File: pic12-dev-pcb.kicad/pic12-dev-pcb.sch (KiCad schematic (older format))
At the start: 8 parts, among them J1 PGM-Conn, J2 App-Conn1, J3 App-Conn2, U1 PIC12F675-ISN

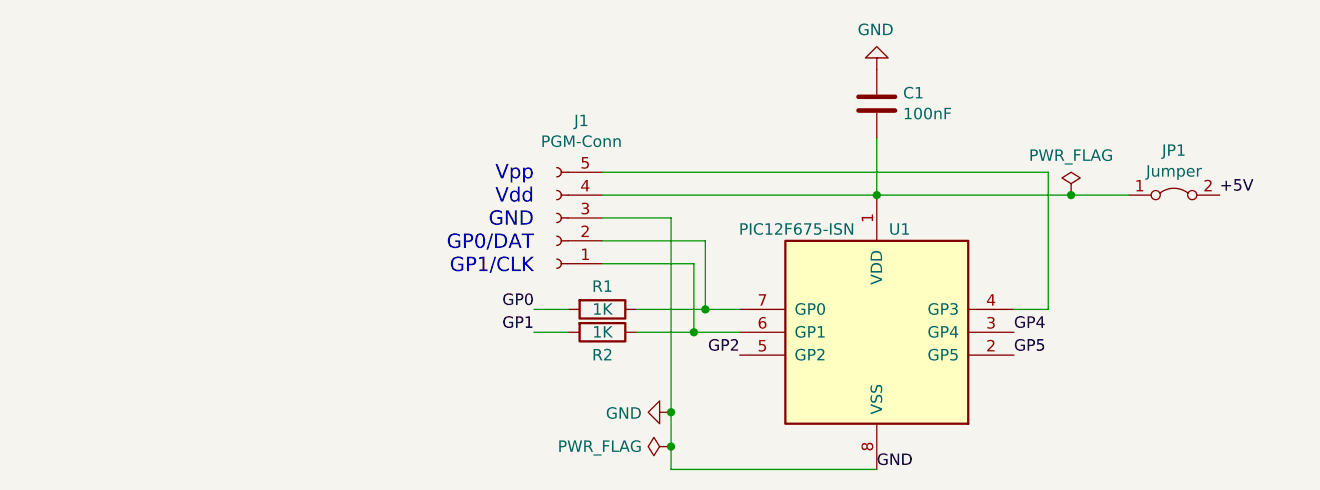
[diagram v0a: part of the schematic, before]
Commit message: added SR-connector
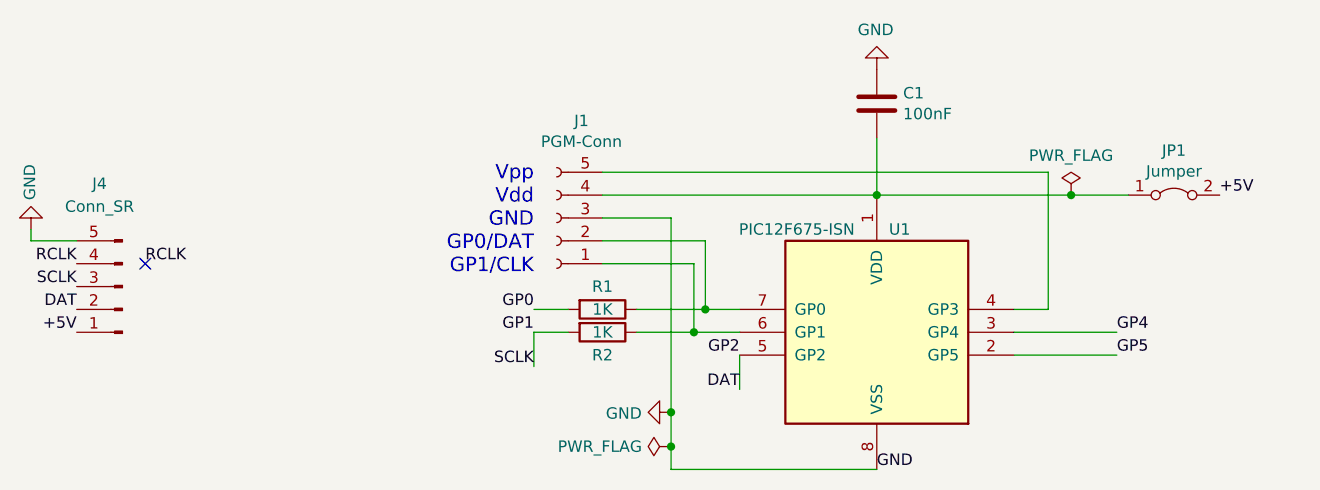
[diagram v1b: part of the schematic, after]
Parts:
- added J4: Conn_SR, Connector_PinHeader_2.54mm:PinHeader_1x05_P2.54mm_Vertical, symbol Connector:Conn_01x05_Male
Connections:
- net +5V: now also J4.1 (Pin_1)
- net GND: now also J4.5 (Pin_5)
- net GP1: now also J4.3 (Pin_3)
- net GP2 renamed DAT
- net DAT: now also J4.2 (Pin_2)
- new net RCLK: J4.4 (Pin_4)
- no-connect marks 0 -> 1
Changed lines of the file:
@@
 Sheet 1 1
 Title "PIC12-Development Breadboard-PCB"
-Date "2020-08-30"
+Date "2020-08-31"
 Rev "1"
 Comp "Bernhard Bablok"
@@
 Text Label 7850 3900 2    50   ~ 0
 GP2
-Text Label 6350 3550 0    50   ~ 0
+Text Label 6800 3550 0    50   ~ 0
 GP4
-Text Label 6350 3650 0    50   ~ 0
+Text Label 6800 3650 0    50   ~ 0
 GP5
 Text Label 5150 3650 2    50   ~ 0
@@
 Text Label 9000 3900 0    50   ~ 0
 GP2
+$Comp
+L Connector:Conn_01x05_Male J4
+U 1 1 5F4D3DB1
+P 2450 3350
+F 0 "J4" H 2550 2900 50  0000 C CNN
+F 1 "Conn_SR" H 2550 3000 50  0000 C CNN
+F 2 "Connector_PinHeader_2.54mm:PinHeader_1x05_P2.54mm_Vertical" H 2450 3350 50  0001 C CNN
+F 3 "~" H 2450 3350 50  0001 C CNN
+	1    2450 3350
+	-1   0    0    1
+$EndComp
+$Comp
+L power:GND #PWR0103
+U 1 1 5F4D4AE2
+P 2050 3100
+F 0 "#PWR0103" H 2050 2850 50  0001 C CNN
+F 1 "GND" V 2055 2972 50  0000 R CNN
+F 2 "" H 2050 3100 50  0001 C CNN
+F 3 "" H 2050 3100 50  0001 C CNN
+	1    2050 3100
+	-1   0    0    1
+$EndComp
+Text Label 2250 3250 2    50   ~ 0
+RCLK
+Text Label 2250 3350 2    50   ~ 0
+SCLK
+Text Label 2250 3450 2    50   ~ 0
+DAT
+Text Label 2250 3550 2    50   ~ 0
++5V
+Wire Wire Line
+	2250 3150 2050 3150
+Wire Wire Line
+	2050 3150 2050 3100
+Wire Wire Line
+	6350 3650 6800 3650
+Wire Wire Line
+	6350 3550 6800 3550
+Text Label 5150 3800 2    50   ~ 0
+DAT
+Wire Wire Line
+	5150 3800 5150 3650
+Text Label 4250 3700 2    50   ~ 0
+SCLK
+Wire Wire Line
+	4250 3700 4250 3550
+Text Label 2550 3250 0    50   ~ 0
+RCLK
+NoConn ~ 2550 3250
 $EndSCHEMATC

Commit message: fix labeling of GP2 net, add USB-connector
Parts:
- added J5: USB_B_Micro, symbol Connector:USB_B_Micro
- added J6: Conn_BB1, Connector_PinHeader_2.54mm:PinHeader_2x01_P2.54mm_Horizontal, symbol Connector:Conn_01x02_Male
- added J7: Conn_BB2, Connector_PinHeader_2.54mm:PinHeader_2x01_P2.54mm_Horizontal, symbol Connector:Conn_01x02_Male
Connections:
- net labels removed: DAT
- wire segments 28 -> 37
- no-connect marks 1 -> 4
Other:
- note added: "SERin"
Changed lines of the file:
@@
 Title "PIC12-Development Breadboard-PCB"
 Date "2020-09-07"
-Rev "2"
+Rev "3"
 Comp "Bernhard Bablok"
 Comment1 "https://github.com/bablokb/pcb-pic-devboard"
@@
 $EndComp
 $Comp
-L power:PWR_FLAG #FLG0102
-U 1 1 5F05C8DC
-P 4850 4050
-F 0 "#FLG0102" H 4850 4125 50  0001 C CNN
-F 1 "PWR_FLAG" V 4850 4177 50  0000 L CNN
-F 2 "" H 4850 4050 50  0001 C CNN
-F 3 "~" H 4850 4050 50  0001 C CNN
-	1    4850 4050
-	0    -1   -1   0
-$EndComp
-Connection ~ 4850 4050
-Wire Wire Line
-	4850 4050 4850 4150
-$Comp
 L Device:C C1
 U 1 1 5F062C50
@@
 L power:GND #PWR0102
 U 1 1 5F0642E9
-P 4850 3900
-F 0 "#PWR0102" H 4850 3650 50  0001 C CNN
-F 1 "GND" V 4855 3772 50  0000 R CNN
-F 2 "" H 4850 3900 50  0001 C CNN
-F 3 "" H 4850 3900 50  0001 C CNN
-	1    4850 3900
+P 5150 5300
+F 0 "#PWR0102" H 5150 5050 50  0001 C CNN
+F 1 "GND" V 5155 5172 50  0000 R CNN
+F 2 "" H 5150 5300 50  0001 C CNN
+F 3 "" H 5150 5300 50  0001 C CNN
+	1    5150 5300
 	0    1    1    0
 $EndComp
@@
 	0    1    1    0
 $EndComp
-Connection ~ 4850 3900
-Wire Wire Line
-	4850 3900 4850 4050
 Wire Wire Line
 	4250 3450 4400 3450
-Wire Wire Line
-	4850 3050 4850 3900
 Wire Wire Line
 	4250 3550 4400 3550
@@
 SCLK
 Text Label 2250 3450 2    50   ~ 0
-DAT
+GP2
 Text Label 2250 3550 2    50   ~ 0
 +5V
@@
 Wire Wire Line
 	6350 3550 6800 3550
-Text Label 5150 3800 2    50   ~ 0
-DAT
-Wire Wire Line
-	5150 3800 5150 3650
 Text Label 4250 3700 2    50   ~ 0
 SCLK
@@
 RCLK
 NoConn ~ 2550 3250
+Text Notes 1850 3450 0    50   ~ 0
+SERin
+$Comp
+L Connector:USB_B_Micro J5
+U 1 1 5F569D9B
+P 5900 5300
+F 0 "J5" V 5911 5630 50  0000 L CNN
+F 1 "USB_B_Micro" V 6002 5630 50  0000 L CNN
+F 2 "" H 6050 5250 50  0001 C CNN
+F 3 "~" H 6050 5250 50  0001 C CNN
+	1    5900 5300
+	0    1    1    0
+$EndComp
+NoConn ~ 5700 5600
+NoConn ~ 5800 5600
+NoConn ~ 5900 5600
+Text Label 6200 5700 0    50   ~ 0
++5V
+Wire Wire Line
+	6200 5700 6100 5700
+Wire Wire Line
+	6100 5700 6100 5600
+Wire Wire Line
+	5500 5300 5400 5300
+Wire Wire Line
+	5500 5200 5400 5200
+Wire Wire Line
+	5400 5200 5400 5300
+Connection ~ 5400 5300
+Wire Wire Line
+	4850 3050 4850 4150
+Wire Wire Line
+	5150 5300 5400 5300
+$Comp
+L Connector:Conn_01x02_Male J6
+U 1 1 5F57072D
+P 1950 4500
+F 0 "J6" H 2050 4800 50  0000 C CNN
+F 1 "Conn_BB1" H 2050 4650 50  0000 C CNN
+F 2 "Connector_PinHeader_2.54mm:PinHeader_2x01_P2.54mm_Horizontal" H 1950 4500 50  0001 C CNN
+F 3 "~" H 1950 4500 50  0001 C CNN
+	1    1950 4500
+	1    0    0    -1
+$EndComp
+$Comp
+L Connector:Conn_01x02_Male J7
+U 1 1 5F570C00
+P 2750 4600
+F 0 "J7" H 2900 4250 50  0000 R CNN
+F 1 "Conn_BB2" H 2950 4350 50  0000 R CNN
+F 2 "Connector_PinHeader_2.54mm:PinHeader_2x01_P2.54mm_Horizontal" H 2750 4600 50  0001 C CNN
+F 3 "~" H 2750 4600 50  0001 C CNN
+	1    2750 4600
+	-1   0    0    1
+$EndComp
+$Comp
+L power:GND #PWR0104
+U 1 1 5F5716E2
+P 2400 4750
+F 0 "#PWR0104" H 2400 4500 50  0001 C CNN
+F 1 "GND" V 2405 4622 50  0000 R CNN
+F 2 "" H 2400 4750 50  0001 C CNN
+F 3 "" H 2400 4750 50  0001 C CNN
+	1    2400 4750
+	0    -1   -1   0
+$EndComp
+Text Label 2250 4750 2    50   ~ 0
++5V
+Wire Wire Line
+	2250 4750 2250 4600
+Wire Wire Line
+	2250 4600 2150 4600
+Wire Wire Line
+	2250 4600 2550 4600
+Connection ~ 2250 4600
+Wire Wire Line
+	2400 4750 2400 4500
+Wire Wire Line
+	2400 4500 2550 4500
+Wire Wire Line
+	2400 4500 2150 4500
+Connection ~ 2400 4500
 $EndSCHEMATC

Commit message: swap GP0-GP2, add micro-USB breakout
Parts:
- removed J5: USB_B_Micro, symbol Connector:USB_B_Micro
- removed J7: Conn_BB2, Connector_PinHeader_2.54mm:PinHeader_2x01_P2.54mm_Horizontal, symbol Connector:Conn_01x02_Male
- added USB1: Micro-USB_Breakout, user:Micro-USB_Breakout, symbol User:Micro-USB_Breakout
- J1: footprint Connector_PinHeader_2.54mm:PinHeader_1x05_P2.54mm_Vertical -> Connector_PinSocket_2.54mm:PinSocket_1x05_P2.54mm_Vertical
- J6: footprint Connector_PinHeader_2.54mm:PinHeader_2x01_P2.54mm_Horizontal -> Connector_PinHeader_2.54mm:PinHeader_1x02_P2.54mm_Horizontal
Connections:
- wire segments 37 -> 33
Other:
- moved on the sheet: J6
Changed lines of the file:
@@
 Sheet 1 1
 Title "PIC12-Development Breadboard-PCB"
-Date "2020-09-07"
+Date "2020-09-19"
 Rev "3"
 Comp "Bernhard Bablok"
@@
 F 0 "J1" H 4242 2625 50  0000 C CNN
 F 1 "PGM-Conn" H 4242 2716 50  0000 C CNN
-F 2 "Connector_PinHeader_2.54mm:PinHeader_1x05_P2.54mm_Vertical" H 4350 3050 50  0001 C CNN
+F 2 "Connector_PinSocket_2.54mm:PinSocket_1x05_P2.54mm_Vertical" H 4350 3050 50  0001 C CNN
 F 3 "~" H 4350 3050 50  0001 C CNN
 	1    4350 3050
@@
 L power:GND #PWR0102
 U 1 1 5F0642E9
-P 5150 5300
-F 0 "#PWR0102" H 5150 5050 50  0001 C CNN
-F 1 "GND" V 5155 5172 50  0000 R CNN
-F 2 "" H 5150 5300 50  0001 C CNN
-F 3 "" H 5150 5300 50  0001 C CNN
-	1    5150 5300
+P 5600 4750
+F 0 "#PWR0102" H 5600 4500 50  0001 C CNN
+F 1 "GND" V 5605 4622 50  0000 R CNN
+F 2 "" H 5600 4750 50  0001 C CNN
+F 3 "" H 5600 4750 50  0001 C CNN
+	1    5600 4750
 	0    1    1    0
 $EndComp
@@
 Text Label 7850 3600 2    50   ~ 0
 GND
-Text Label 7850 3700 2    50   ~ 0
+Text Label 7850 3900 2    50   ~ 0
 GP0
 Text Label 7850 3800 2    50   ~ 0
 GP1
-Text Label 7850 3900 2    50   ~ 0
+Text Label 7850 3700 2    50   ~ 0
 GP2
 Text Label 6800 3550 0    50   ~ 0
@@
 Text Label 8500 3600 2    50   ~ 0
 GND
-Text Label 8500 3700 2    50   ~ 0
+Text Label 8500 3900 2    50   ~ 0
 GP0
 Text Label 8500 3800 2    50   ~ 0
 GP1
-Text Label 8500 3900 2    50   ~ 0
+Text Label 8500 3700 2    50   ~ 0
 GP2
 $Comp
@@
 Text Label 9000 3600 0    50   ~ 0
 GND
-Text Label 9000 3700 0    50   ~ 0
+Text Label 9000 3900 0    50   ~ 0
 GP0
 Text Label 9000 3800 0    50   ~ 0
 GP1
-Text Label 9000 3900 0    50   ~ 0
-GP2
+Text Label 9000 3700 0    50   ~ 0
+GP2
+$Comp
+L power:GND #PWR0103
+U 1 1 5F4D4AE2
+P 2050 3100
+F 0 "#PWR0103" H 2050 2850 50  0001 C CNN
+F 1 "GND" V 2055 2972 50  0000 R CNN
+F 2 "" H 2050 3100 50  0001 C CNN
+F 3 "" H 2050 3100 50  0001 C CNN
+	1    2050 3100
+	-1   0    0    1
+$EndComp
+Text Label 2250 3250 2    50   ~ 0
+RCLK
+Text Label 2250 3350 2    50   ~ 0
+SCLK
+Text Label 2250 3450 2    50   ~ 0
+GP2
+Text Label 2250 3550 2    50   ~ 0
++5V
+Wire Wire Line
+	2250 3150 2050 3150
+Wire Wire Line
+	2050 3150 2050 3100
+Wire Wire Line
+	6350 3650 6800 3650
+Wire Wire Line
+	6350 3550 6800 3550
+Text Label 4250 3700 2    50   ~ 0
+SCLK
+Wire Wire Line
+	4250 3700 4250 3550
+Text Label 2550 3250 0    50   ~ 0
+RCLK
+NoConn ~ 2550 3250
+Text Notes 1850 3450 0    50   ~ 0
+SERin
+Text Label 5600 5150 2    50   ~ 0
++5V
+Wire Wire Line
+	4850 3050 4850 4150
+$Comp
+L Connector:Conn_01x02_Male J6
+U 1 1 5F57072D
+P 4600 5000
+F 0 "J6" H 4700 5300 50  0000 C CNN
+F 1 "Conn_BB1" H 4700 5150 50  0000 C CNN
+F 2 "Connector_PinHeader_2.54mm:PinHeader_1x02_P2.54mm_Horizontal" H 4600 5000 50  0001 C CNN
+F 3 "~" H 4600 5000 50  0001 C CNN
+	1    4600 5000
+	1    0    0    1
+$EndComp
+$Comp
+L User:Micro-USB_Breakout USB1
+U 1 1 5F660F6B
+P 6100 4950
+F 0 "USB1" H 6327 4992 50  0000 L CNN
+F 1 "Micro-USB_Breakout" H 6327 4901 50  0000 L CNN
+F 2 "user:Micro-USB_Breakout" H 6100 4950 50  0001 C CNN
+F 3 "~" H 6100 4950 50  0001 C CNN
+	1    6100 4950
+	1    0    0    -1
+$EndComp
+NoConn ~ 5900 4850
+NoConn ~ 5900 4950
+NoConn ~ 5900 5050
+Wire Wire Line
+	5600 4750 5750 4750
+Wire Wire Line
+	5900 5150 5750 5150
+$Comp
+L power:PWR_FLAG #FLG0102
+U 1 1 5F6670F7
+P 5750 4750
+F 0 "#FLG0102" H 5750 4825 50  0001 C CNN
+F 1 "PWR_FLAG" H 5750 4923 50  0000 C CNN
+F 2 "" H 5750 4750 50  0001 C CNN
+F 3 "~" H 5750 4750 50  0001 C CNN
+	1    5750 4750
+	1    0    0    -1
+$EndComp
+Connection ~ 5750 4750
+Wire Wire Line
+	5750 4750 5900 4750
+$Comp
+L power:PWR_FLAG #FLG0103
+U 1 1 5F6676D5
+P 5750 5150
+F 0 "#FLG0103" H 5750 5225 50  0001 C CNN
+F 1 "PWR_FLAG" H 5750 5323 50  0000 C CNN
+F 2 "" H 5750 5150 50  0001 C CNN
+F 3 "~" H 5750 5150 50  0001 C CNN
+	1    5750 5150
+	-1   0    0    1
+$EndComp
+Connection ~ 5750 5150
+Wire Wire Line
+	5750 5150 5600 5150
+Wire Wire Line
+	5750 4900 5750 4750
+Wire Wire Line
+	4800 4900 5750 4900
+Wire Wire Line
+	5750 5150 5750 5000
+Wire Wire Line
+	4800 5000 5750 5000
 $Comp
 L Connector:Conn_01x05_Male J4
@@
 	-1   0    0    1
 $EndComp
-$Comp
-L power:GND #PWR0103
-U 1 1 5F4D4AE2
-P 2050 3100
-F 0 "#PWR0103" H 2050 2850 50  0001 C CNN
-F 1 "GND" V 2055 2972 50  0000 R CNN
-F 2 "" H 2050 3100 50  0001 C CNN
-F 3 "" H 2050 3100 50  0001 C CNN
-	1    2050 3100
-	-1   0    0    1
-$EndComp
-Text Label 2250 3250 2    50   ~ 0
-RCLK
-Text Label 2250 3350 2    50   ~ 0
-SCLK
-Text Label 2250 3450 2    50   ~ 0
-GP2
-Text Label 2250 3550 2    50   ~ 0
-+5V
-Wire Wire Line
-	2250 3150 2050 3150
-Wire Wire Line
-	2050 3150 2050 3100
-Wire Wire Line
-	6350 3650 6800 3650
-Wire Wire Line
-	6350 3550 6800 3550
-Text Label 4250 3700 2    50   ~ 0
-SCLK
-Wire Wire Line
-	4250 3700 4250 3550
-Text Label 2550 3250 0    50   ~ 0
-RCLK
-NoConn ~ 2550 3250
-Text Notes 1850 3450 0    50   ~ 0
-SERin
-$Comp
-L Connector:USB_B_Micro J5
-U 1 1 5F569D9B
-P 5900 5300
-F 0 "J5" V 5911 5630 50  0000 L CNN
-F 1 "USB_B_Micro" V 6002 5630 50  0000 L CNN
-F 2 "" H 6050 5250 50  0001 C CNN
-F 3 "~" H 6050 5250 50  0001 C CNN
-	1    5900 5300
-	0    1    1    0
-$EndComp
-NoConn ~ 5700 5600
-NoConn ~ 5800 5600
-NoConn ~ 5900 5600
-Text Label 6200 5700 0    50   ~ 0
-+5V
-Wire Wire Line
-	6200 5700 6100 5700
-Wire Wire Line
-	6100 5700 6100 5600
-Wire Wire Line
-	5500 5300 5400 5300
-Wire Wire Line
-	5500 5200 5400 5200
-Wire Wire Line
-	5400 5200 5400 5300
-Connection ~ 5400 5300
-Wire Wire Line
-	4850 3050 4850 4150
-Wire Wire Line
-	5150 5300 5400 5300
-$Comp
-L Connector:Conn_01x02_Male J6
-U 1 1 5F57072D
-P 1950 4500
-F 0 "J6" H 2050 4800 50  0000 C CNN
-F 1 "Conn_BB1" H 2050 4650 50  0000 C CNN
-F 2 "Connector_PinHeader_2.54mm:PinHeader_2x01_P2.54mm_Horizontal" H 1950 4500 50  0001 C CNN
-F 3 "~" H 1950 4500 50  0001 C CNN
-	1    1950 4500
-	1    0    0    -1
-$EndComp
-$Comp
-L Connector:Conn_01x02_Male J7
-U 1 1 5F570C00
-P 2750 4600
-F 0 "J7" H 2900 4250 50  0000 R CNN
-F 1 "Conn_BB2" H 2950 4350 50  0000 R CNN
-F 2 "Connector_PinHeader_2.54mm:PinHeader_2x01_P2.54mm_Horizontal" H 2750 4600 50  0001 C CNN
-F 3 "~" H 2750 4600 50  0001 C CNN
-	1    2750 4600
-	-1   0    0    1
-$EndComp
-$Comp
-L power:GND #PWR0104
-U 1 1 5F5716E2
-P 2400 4750
-F 0 "#PWR0104" H 2400 4500 50  0001 C CNN
-F 1 "GND" V 2405 4622 50  0000 R CNN
-F 2 "" H 2400 4750 50  0001 C CNN
-F 3 "" H 2400 4750 50  0001 C CNN
-	1    2400 4750
-	0    -1   -1   0
-$EndComp
-Text Label 2250 4750 2    50   ~ 0
-+5V
-Wire Wire Line
-	2250 4750 2250 4600
-Wire Wire Line
-	2250 4600 2150 4600
-Wire Wire Line
-	2250 4600 2550 4600
-Connection ~ 2250 4600
-Wire Wire Line
-	2400 4750 2400 4500
-Wire Wire Line
-	2400 4500 2550 4500
-Wire Wire Line
-	2400 4500 2150 4500
-Connection ~ 2400 4500
 $EndSCHEMATC

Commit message: changed SO-8 footprint to handsolder-version
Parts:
- U1: footprint Package_SO:SOIC-8_3.9x4.9mm_P1.27mm -> user:SO-8_3.9x4.9mm_P1.27mm_HandSolder
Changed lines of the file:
@@
 Sheet 1 1
 Title "PIC12-Development Breadboard-PCB"
-Date "2020-09-19"
+Date "2020-09-25"
 Rev "3"
 Comp "Bernhard Bablok"
@@
 F 0 "U1" H 5850 4000 50  0000 C CNN
 F 1 "PIC12F675-ISN" H 5400 4000 50  0000 C CNN
-F 2 "Package_SO:SOIC-8_3.9x4.9mm_P1.27mm" H 6350 4200 50  0001 C CNN
+F 2 "user:SO-8_3.9x4.9mm_P1.27mm_HandSolder" H 6350 4200 50  0001 C CNN
 F 3 "http://ww1.microchip.com/downloads/en/DeviceDoc/41190G.pdf" H 5750 3550 50  0001 C CNN
 	1    5750 3550

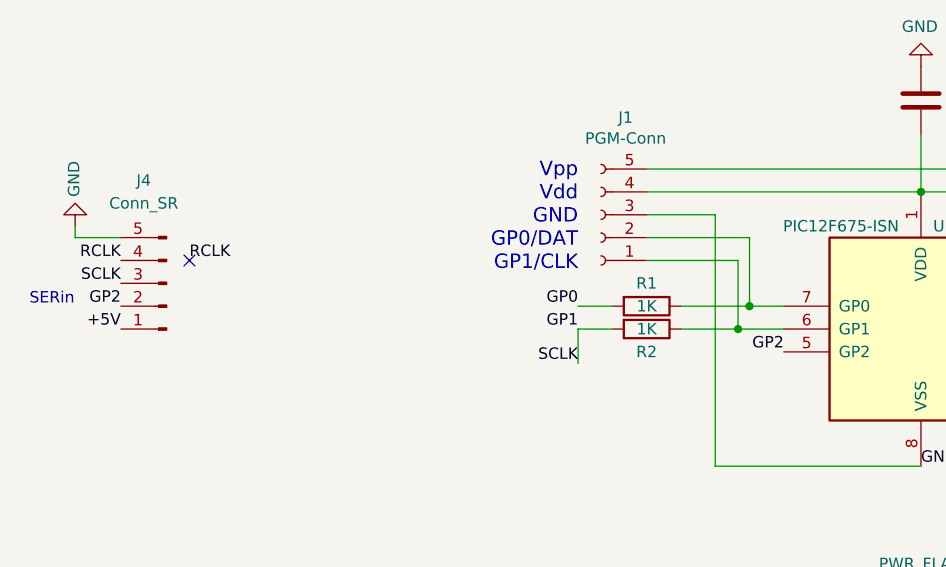
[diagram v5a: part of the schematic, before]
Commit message: Rev4: fixed order of pins of SR-connector
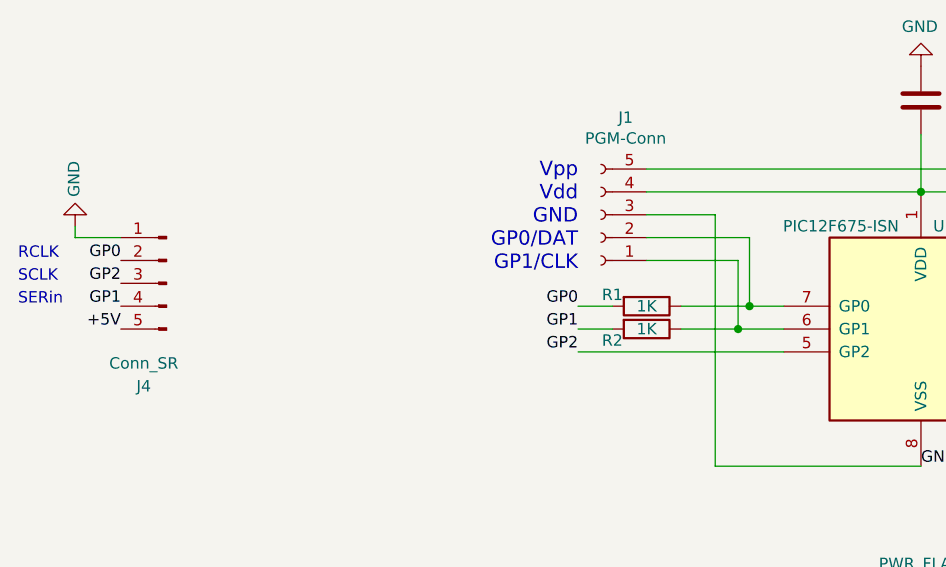
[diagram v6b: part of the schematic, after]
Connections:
- net RCLK is gone; now on net GP1: J4.4 (Pin_4)
- net +5V: now also J4.5 (Pin_5); no longer J4.1 (Pin_1)
- net GND: now also J4.1 (Pin_1); no longer J4.5 (Pin_5)
- net GP0: now also J4.2 (Pin_2)
- net GP1: no longer J4.3 (Pin_3)
- net GP2: now also J4.3 (Pin_3); no longer J4.2 (Pin_2)
- no-connect marks 4 -> 3
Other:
- note added: "RCLK"
- note added: "SCLK"
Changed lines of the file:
@@
 Sheet 1 1
 Title "PIC12-Development Breadboard-PCB"
-Date "2020-09-25"
-Rev "3"
+Date "2020-10-28"
+Rev "4"
 Comp "Bernhard Bablok"
 Comment1 "https://github.com/bablokb/pcb-pic-devboard"
@@
 Text Label 6800 3650 0    50   ~ 0
 GP5
-Text Label 5150 3650 2    50   ~ 0
+Text Label 4250 3650 2    50   ~ 0
 GP2
 Text Label 7250 2950 0    50   ~ 0
@@
 U 1 1 5F4BA8C0
 P 4550 3450
-F 0 "R1" V 4450 3450 50  0000 C CNN
+F 0 "R1" V 4500 3300 50  0000 C CNN
 F 1 "1K" V 4550 3450 50  0000 C CNN
 F 2 "Resistor_SMD:R_1206_3216Metric_Pad1.42x1.75mm_HandSolder" V 4480 3450 50  0001 C CNN
@@
 U 1 1 5F4BAC46
 P 4550 3550
-F 0 "R2" V 4650 3550 50  0000 C CNN
+F 0 "R2" V 4600 3400 50  0000 C CNN
 F 1 "1K" V 4550 3550 50  0000 C CNN
 F 2 "Resistor_SMD:R_1206_3216Metric_Pad1.42x1.75mm_HandSolder" V 4480 3550 50  0001 C CNN
@@
 $EndComp
 Text Label 2250 3250 2    50   ~ 0
-RCLK
+GP0
 Text Label 2250 3350 2    50   ~ 0
-SCLK
+GP2
 Text Label 2250 3450 2    50   ~ 0
-GP2
+GP1
 Text Label 2250 3550 2    50   ~ 0
 +5V
@@
 Wire Wire Line
 	6350 3550 6800 3550
-Text Label 4250 3700 2    50   ~ 0
-SCLK
-Wire Wire Line
-	4250 3700 4250 3550
-Text Label 2550 3250 0    50   ~ 0
-RCLK
-NoConn ~ 2550 3250
-Text Notes 1850 3450 0    50   ~ 0
+Text Notes 1800 3450 0    50   ~ 0
 SERin
 Text Label 5600 5150 2    50   ~ 0
@@
 F 3 "~" H 2450 3350 50  0001 C CNN
 	1    2450 3350
-	-1   0    0    1
-$EndComp
+	-1   0    0    -1
+$EndComp
+Text Notes 1800 3250 0    50   ~ 0
+RCLK
+Text Notes 1800 3350 0    50   ~ 0
+SCLK
+Wire Wire Line
+	5150 3650 4250 3650
 $EndSCHEMATC
